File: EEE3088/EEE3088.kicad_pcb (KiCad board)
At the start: 2 copper layers, 100 x 100 mm, 74 parts, among them J1 MICROXNJ, Q1 MMDT2222A, U1 HT7533-1, U2 HT7533-1, U3 LTR-303ALS-01, U4 LTR-303ALS-01, U5 Header, U6 AT24C256C-SSHL-T, U7 CH340G, U8 TP4056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

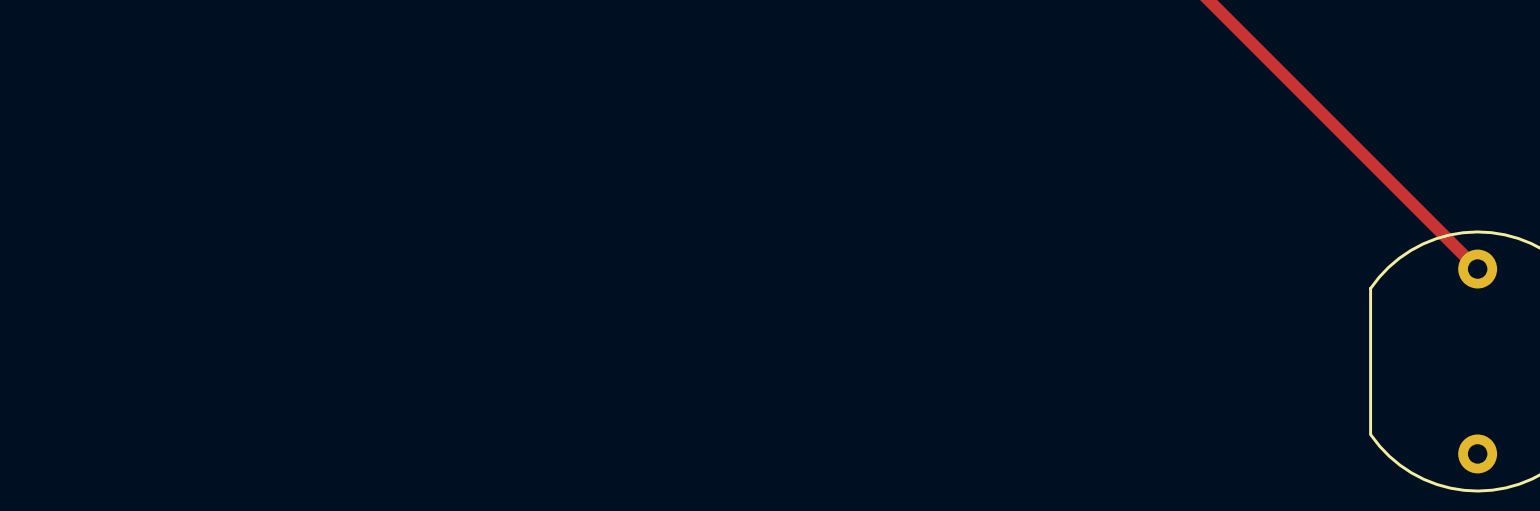
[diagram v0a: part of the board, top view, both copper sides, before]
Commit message: Silkscreen changes
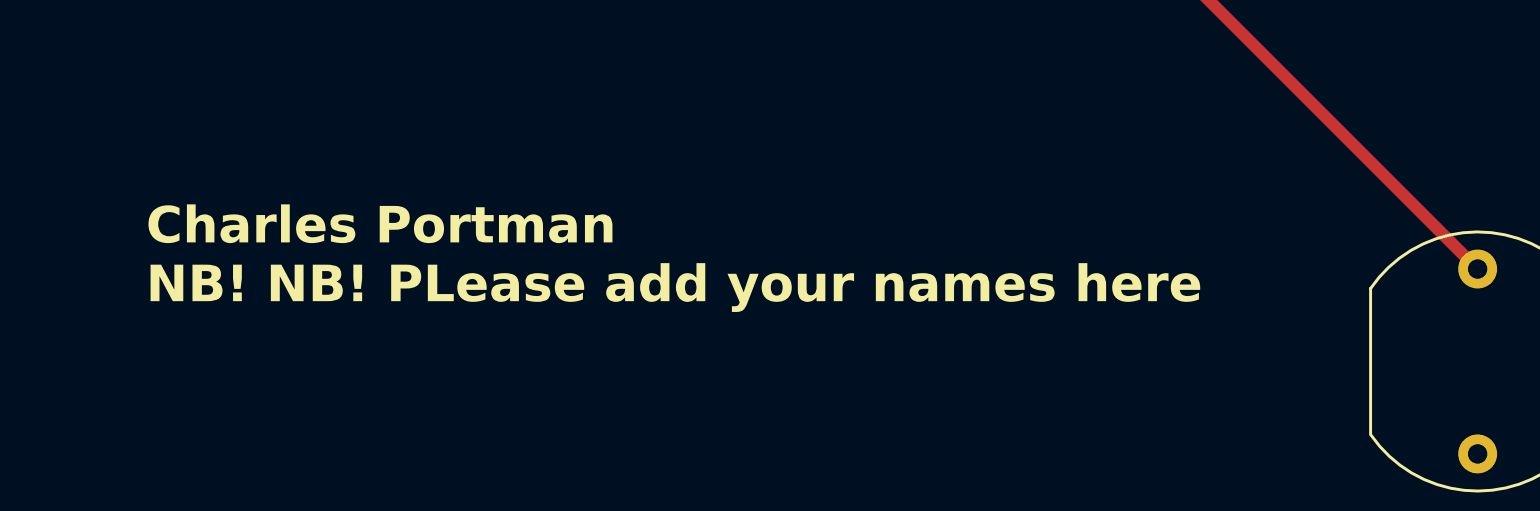
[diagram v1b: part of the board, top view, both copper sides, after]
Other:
- board text added: "Charles Portman NB! NB! PLease add your names here"
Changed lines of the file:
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@@
   (gr_line (start 55 50) (end 145 50)
     (stroke (width 0.1) (type default)) (layer "Edge.Cuts"))
+  (gr_text "Charles Portman\nNB! NB! PLease add your names here" (at 89.281 140.208) (layer "F.SilkS")
+    (effects (font (size 1.5 1.5) (thickness 0.3) bold) (justify left bottom))
+  )
   (segment (start -147.066 35.54) (end -147.066 25.160659) (width 0.5) (layer "F.Cu") (net 0))
   (segment (start -150.464 38.938) (end -147.066 35.54) (width 0.5) (layer "F.Cu") (net 0))

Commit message: PCB - POwer and MCU added
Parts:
- moved R29 305.4 mm to (134.9, 71.1), turned to 180 degrees
- moved R30 269.4 mm to (124.5, 74.9)
- moved U6 269.0 mm to (130.6, 63.6), turned to -90 degrees
- moved C5 257.7 mm to (105.4, 97.7)
- moved C6 257.7 mm to (102.9, 97.7)
- moved C7 257.7 mm to (97.8, 97.7)
- moved C8 257.7 mm to (108.0, 97.7)
- moved C9 257.7 mm to (100.3, 97.7)
- moved R28 236.5 mm to (77.1, 65.4), turned to -90 degrees
- moved R31 229.4 mm to (74.7, 65.4), turned to 90 degrees
- moved J1 215.0 mm to (66.6, 50.1)
- moved TP17 134.6 mm to (59.6, 66.3)
- moved U7 114.3 mm to (67.9, 67.4), turned to -90 degrees
- moved TP16 112.7 mm to (128.3, 74.7), turned to -90 degrees
- moved TP15 112.5 mm to (131.1, 71.2), turned to 90 degrees
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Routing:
- net +3.3V: track 72.1 -> 230.4 mm, vias 2 -> 0
- net GND: track 90.5 -> 24.7 mm
- net (no net): track 49.7 -> 0.00 mm, vias 2 -> 4
- net Net-(Q1B-E2): track 0.00 -> 49.3 mm
- net /Microcontroller/LDR_Vout1: track 46.7 -> 0.00 mm
- net Net-(Q1A-E1): track 0.00 -> 36.3 mm
- net /Microcontroller/EEPROM_SDA: track 0.00 -> 35.9 mm
- net /Microcontroller/SDASense_1: track 34.5 -> 0.26 mm
- net /Microcontroller/LDR_Vout2: track 34.0 -> 0.00 mm
- net /Power_Subsystem/V-pos: track 0.00 -> 31.0 mm
- net Net-(U9-VOUTA): track 0.00 -> 28.4 mm
- net +3V3: track 31.7 -> 6.53 mm, vias 2 -> 0
- net +5V: track 28.4 -> 49.3 mm
- net /Power_Subsystem/Vbat: track 0.00 -> 18.3 mm, vias 0 -> 1
- net /Microcontroller/EEPROM_SCL: track 28.0 -> 44.1 mm
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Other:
- outline, holes or cut-outs redrawn

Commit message: PCB-Final
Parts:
- moved TP14 2.29 mm to (59.7, 90.4)
- moved TP11 1.20 mm to (143.6, 90.7)
- moved R10 0.68 mm to (99.2, 132.5)
- moved R9 0.68 mm to (105.2, 132.6)
- moved TP7 0.68 mm to (95.2, 132.8)
- renumbered N-Mos1 to N1, P-Mos1 to P1
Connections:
- R29 pad 1: +3V3 -> +3.3V
- R30 pad 1: +3V3 -> +3.3V
- R31 pad 1: +3V3 -> +3.3V
- U5 pad 10: unconnected-(U5-PA0-Pad10) -> /Microcontroller/LDR_Vout2
- U5 pad 12: /Microcontroller/LDR_Vout2 -> unconnected-(U5-PA2-Pad12)
- U5 pad 16: /Microcontroller/USB_TIMIN -> unconnected-(U5-PA6-Pad16)
- U5 pad 45: unconnected-(U5-PB8-Pad45) -> /Microcontroller/USB_TIMIN
- U6 pad 8: +3V3 -> +3.3V
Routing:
- net +3.3V: track 230.4 -> 428.1 mm, vias 0 -> 2
- net /Microcontroller/SCLSense: track 0.00 -> 105.9 mm, vias 0 -> 5
- net /Microcontroller/SDASense_1: track 0.26 -> 105.5 mm, vias 0 -> 4
- net +5V: track 49.3 -> 129.5 mm, vias 0 -> 2
- net /Microcontroller/USB_RXD: track 0.00 -> 74.8 mm, vias 0 -> 3
- net /Microcontroller/USB_TXD: track 0.00 -> 67.7 mm, vias 0 -> 3
- net /Microcontroller/LDR_Vout1: track 0.00 -> 65.1 mm, vias 0 -> 2
- net /Microcontroller/LDR_Vout2: track 0.00 -> 58.0 mm, vias 0 -> 2
- net /Microcontroller/Analogue_Enable1: track 0.00 -> 53.3 mm, vias 0 -> 1
- net /Microcontroller/Analogue_Enable2: track 0.00 -> 49.8 mm, vias 0 -> 3
- net /Power_Subsystem/V-Reg: track 0.00 -> 31.8 mm, vias 0 -> 3
- net /Microcontroller/USB_TIMIN: track 10.4 -> 42.0 mm
- net GND: track 24.7 -> 56.3 mm, vias 2 -> 9
- net /Power_Subsystem/3.3-back: track 0.55 -> 27.0 mm, vias 0 -> 2
- net Net-(U7-V3): track 11.0 -> 19.6 mm
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- added copper zone on B.Cu, net GND
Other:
- board text added: "Charles Portman"
- board text added: "GND"
- board text added: "NB! NB! Please add your names here"
- board text removed: "Charles Portman NB! NB! PLease add your names here"

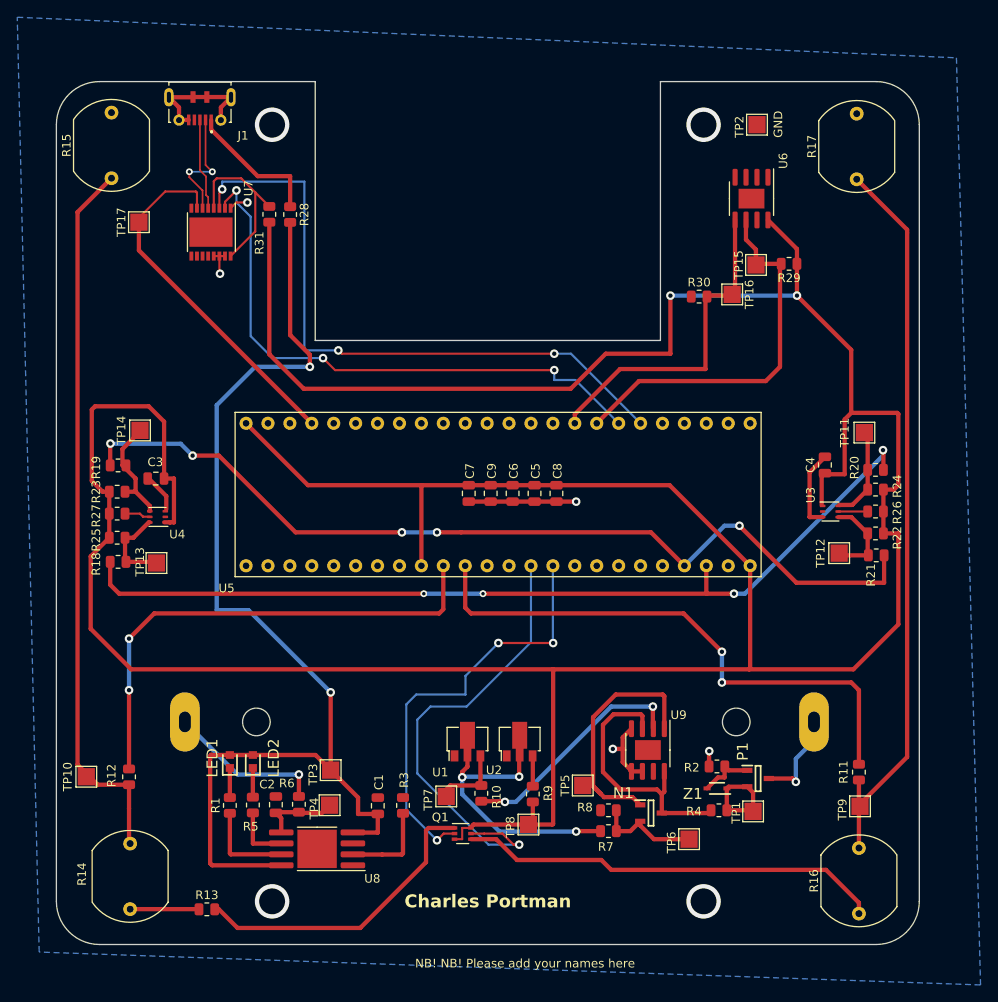
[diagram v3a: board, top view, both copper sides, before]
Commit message: GND connections updated
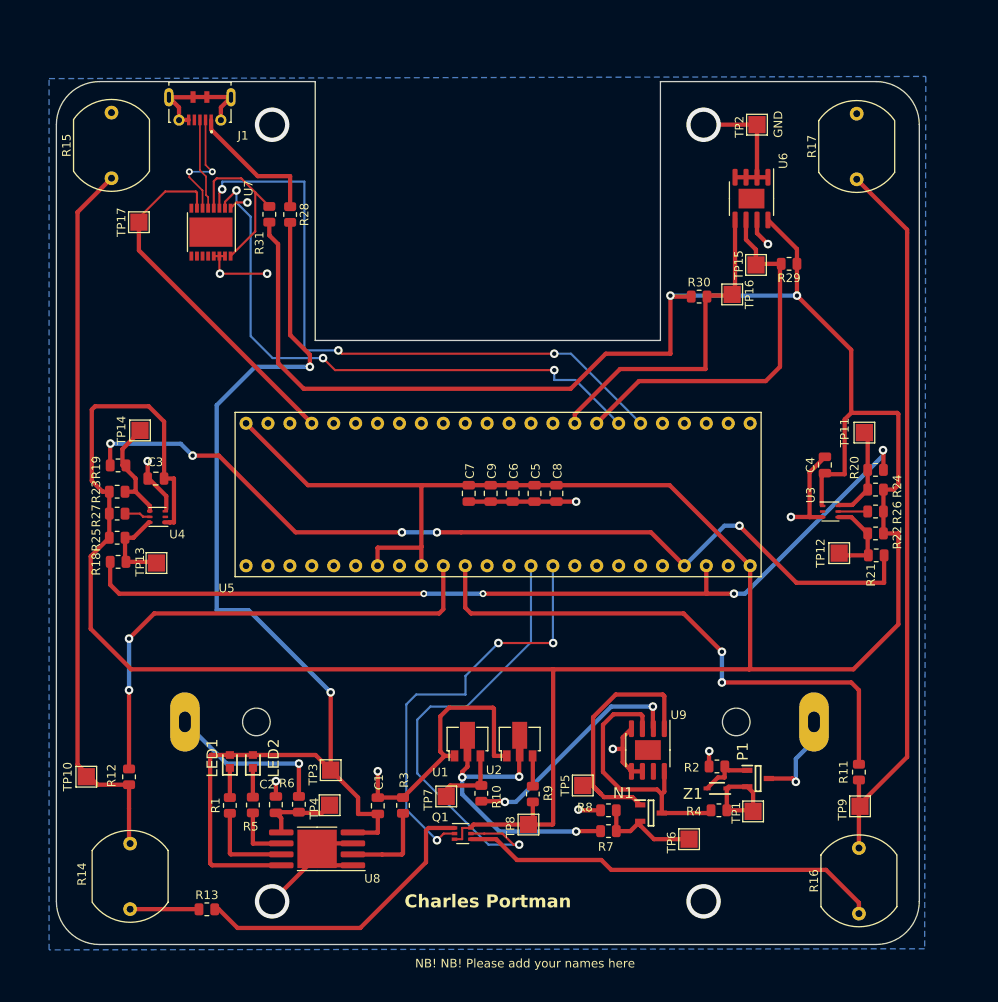
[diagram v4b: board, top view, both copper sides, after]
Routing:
- net GND: track 56.3 -> 139.7 mm, vias 9 -> 16
- net +3.3V: track 428.1 -> 437.7 mm
- net /Power_Subsystem/Vbat: track 18.3 -> 19.0 mm

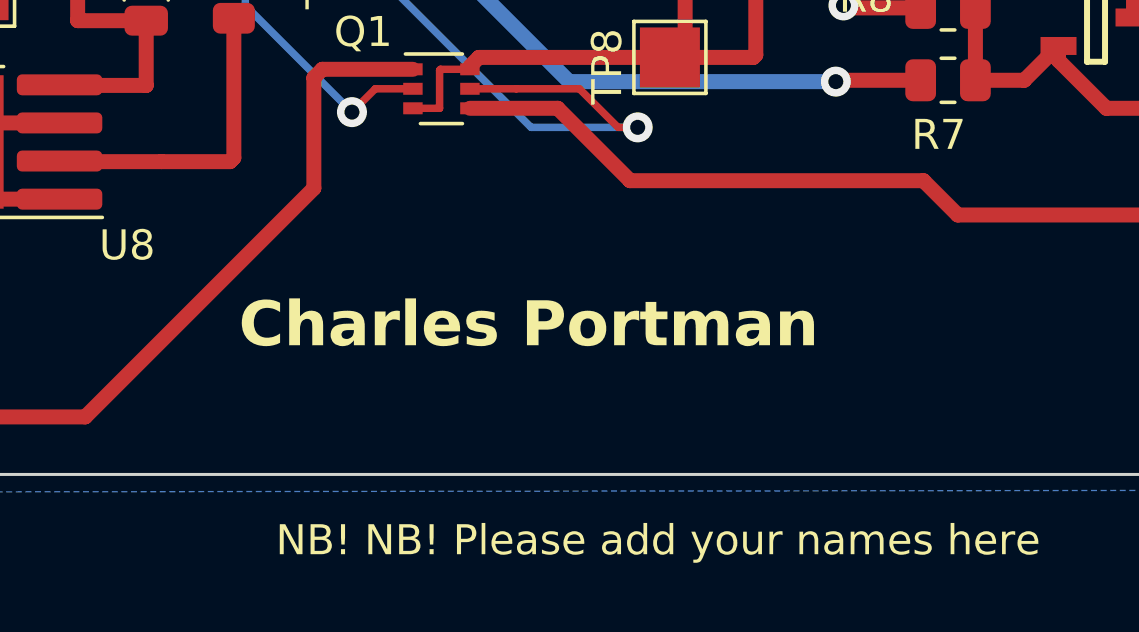
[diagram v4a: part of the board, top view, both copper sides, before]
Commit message: Added group number and names
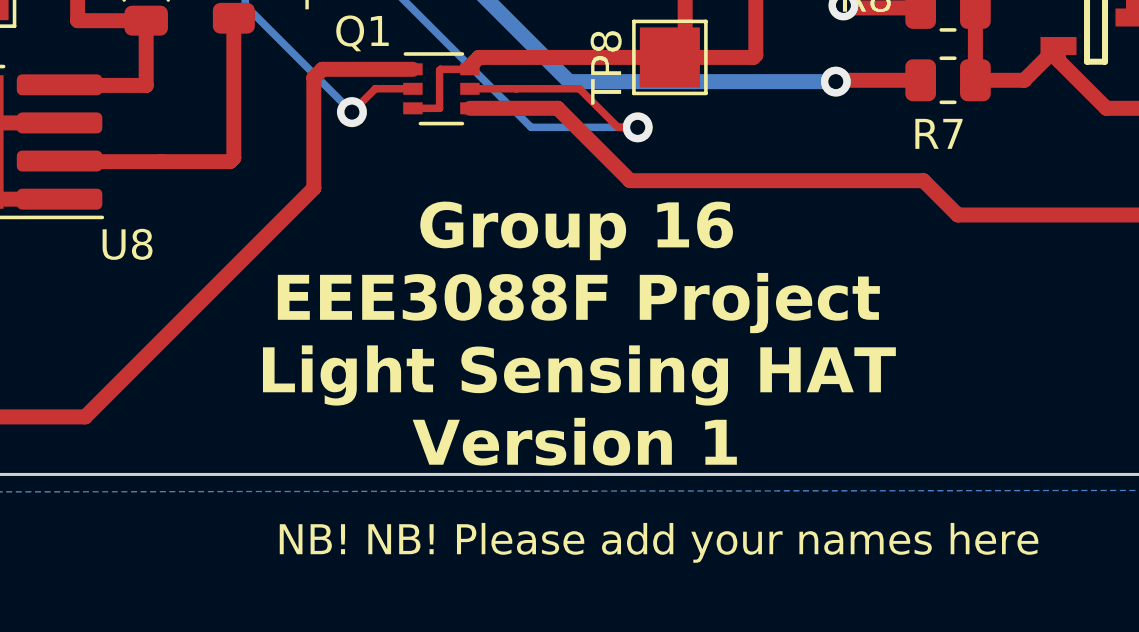
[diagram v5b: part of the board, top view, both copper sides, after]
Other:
- board text added: "By: Charles Portman Jack Youens Jake Wesselink"
- board text added: "Group 16 EEE3088F Project Light Sensing HAT Version 1"
- board text removed: "Charles Portman"
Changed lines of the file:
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@@
   (gr_line (start 120 50) (end 145 50)
     (stroke (width 0.1) (type default)) (layer "Edge.Cuts"))
+  (gr_text "By: \nCharles Portman\nJack Youens\nJake Wesselink" (at 99.06 149.86) (layer "B.SilkS")
+    (effects (font (size 1.5 1.5) (thickness 0.3) bold) (justify bottom))
+  )
+  (gr_text "Group 16\nEEE3088F Project\nLight Sensing HAT \nVersion 1" (at 101.6 149.86) (layer "F.SilkS")
+    (effects (font (size 1.5 1.5) (thickness 0.3) bold) (justify bottom))
+  )
   (gr_text "NB! NB! Please add your names here\n" (at 91.567 152.781) (layer "F.SilkS")
     (effects (font (size 1 1) (thickness 0.15)) (justify left bottom))
   )
-  (gr_text "Charles Portman" (at 100 145) (layer "F.SilkS")
-    (effects (font (size 1.5 1.5) (thickness 0.3) bold))
-  )
   (gr_text "GND" (at 134.239 56.515 90) (layer "F.SilkS")

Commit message: Fixed Text
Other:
- board text added: "Charles Portman Jack Youens Jake Wesselink"
- board text removed: "By: Charles Portman Jack Youens Jake Wesselink"
- board text removed: "NB! NB! Please add your names here"
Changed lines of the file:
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@@
   (gr_line (start 120 50) (end 145 50)
     (stroke (width 0.1) (type default)) (layer "Edge.Cuts"))
-  (gr_text "By: \nCharles Portman\nJack Youens\nJake Wesselink" (at 99.06 149.86) (layer "B.SilkS")
-    (effects (font (size 1.5 1.5) (thickness 0.3) bold) (justify bottom))
+  (gr_text "Charles Portman\nJack Youens\nJake Wesselink" (at 100 148) (layer "B.SilkS")
+    (effects (font (size 1.5 1.5) (thickness 0.3) bold) (justify bottom mirror))
   )
-  (gr_text "Group 16\nEEE3088F Project\nLight Sensing HAT \nVersion 1" (at 101.6 149.86) (layer "F.SilkS")
-    (effects (font (size 1.5 1.5) (thickness 0.3) bold) (justify bottom))
-  )
-  (gr_text "NB! NB! Please add your names here\n" (at 91.567 152.781) (layer "F.SilkS")
-    (effects (font (size 1 1) (thickness 0.15)) (justify left bottom))
+  (gr_text "Group 16\nEEE3088F Project\nLight Sensing HAT \nVersion 1" (at 100 145) (layer "F.SilkS")
+    (effects (font (size 1.5 1.5) (thickness 0.3) bold))
   )
   (gr_text "GND" (at 134.239 56.515 90) (layer "F.SilkS")
